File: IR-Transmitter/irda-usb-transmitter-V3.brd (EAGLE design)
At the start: 65.6 x 51 mm, 24 parts, among them IC1 7805, Q2 7.3728MHz, U1 FT232RL, U2 MCP2120

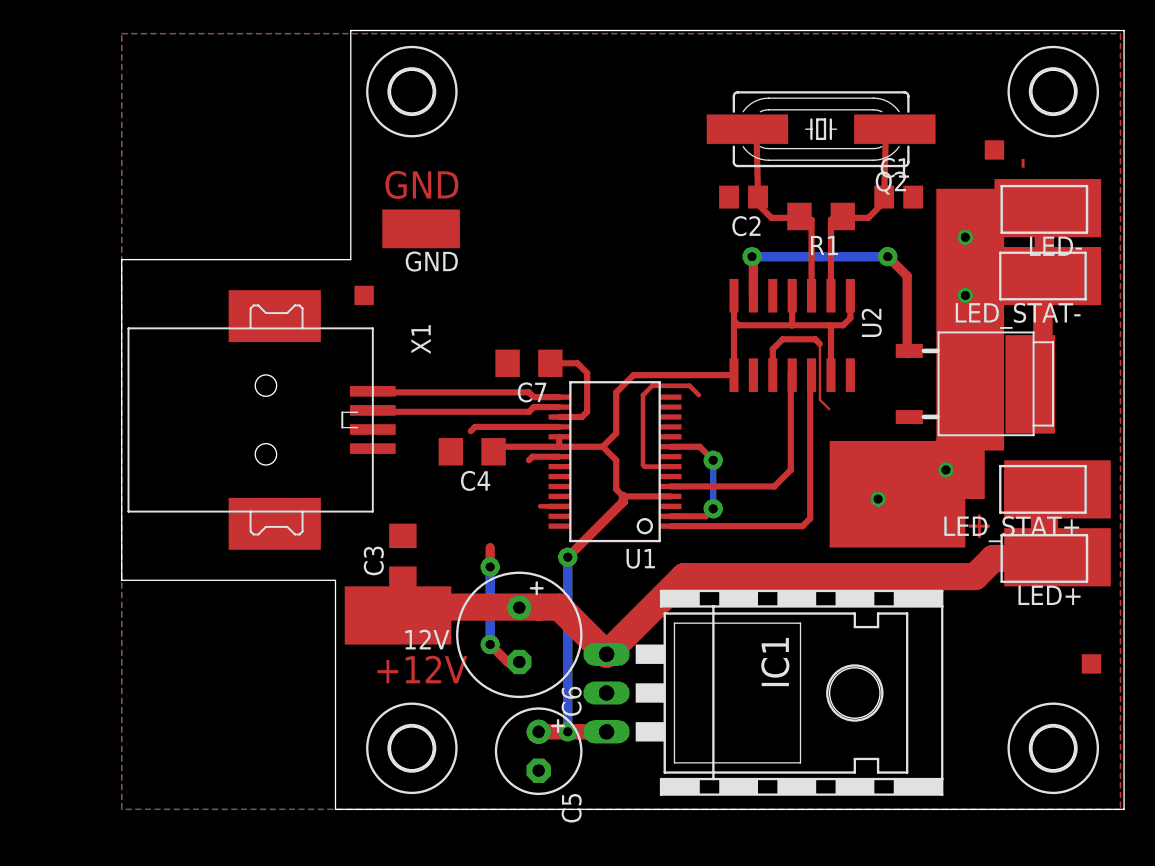
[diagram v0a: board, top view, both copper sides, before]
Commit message: Changed size of IR_Transmitter to fit dirtypcbs.com 50x50mm size.
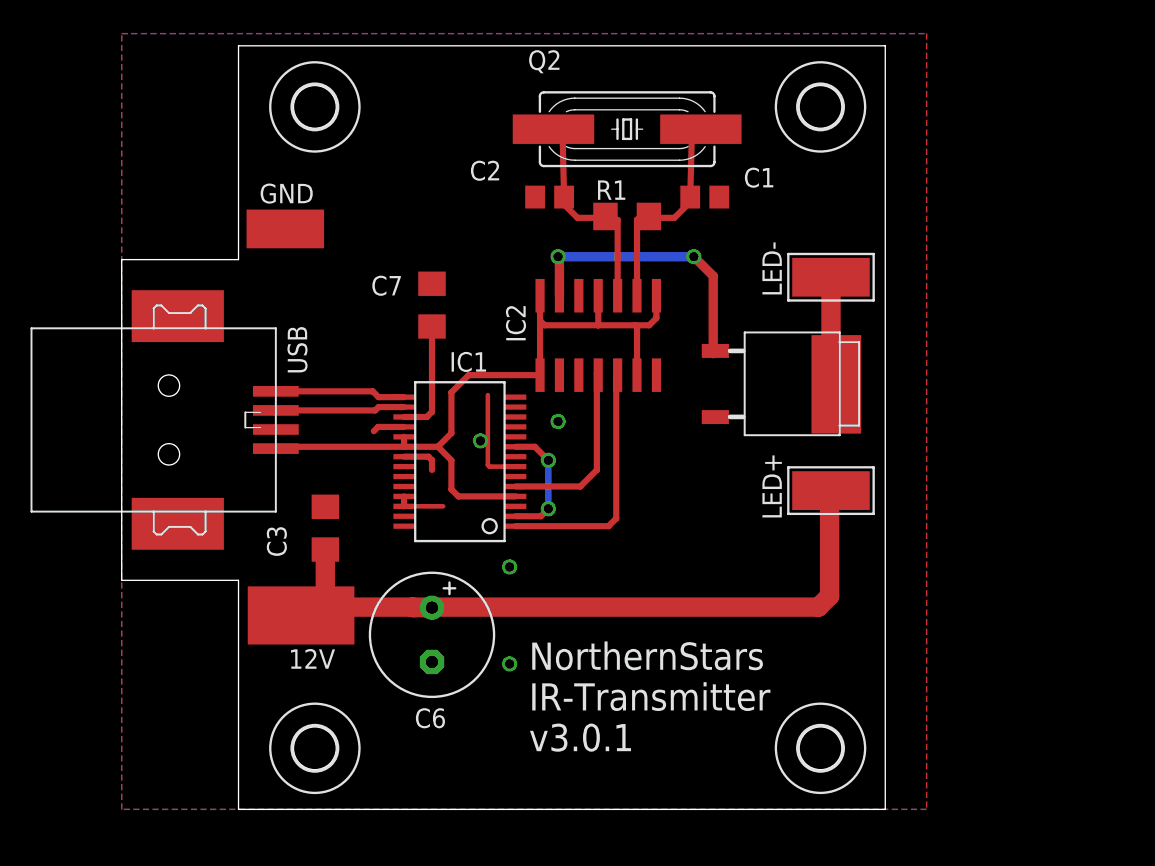
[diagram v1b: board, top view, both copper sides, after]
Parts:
- removed C4: 100n, rcl:C1206
- removed C5: 4µ7, rcl:E2,5-6
- removed LED_STAT+, LED_STAT-: IR-LED, wirepad:5-2,5
- removed U1: FT232RL, ftdichip-3:SSOP28DB
- removed U2: MCP2120, microchip:SO-14
- removed X1: (no value), con-usb-3:USB-B-SMT
- added IC2: MCP2120, microchip:SO-14
- added USB: (no value), con-usb-3:USB-B-SMT
- IC1: value 7805 -> FT232RL; device 78xx_with_heatsink:78XXH -> ftdichip-3:SSOP28DB
- moved IC1 21.1 mm to (22.1, 22.8), turned to 90 degrees
- moved H1 15.3 mm to (45.8, 46.0)
- moved H4 15.2 mm to (45.8, 4.00)
- moved LED+ 14.7 mm to (46.4, 20.9)
- moved LED- 14.7 mm to (46.4, 34.8)
- moved C1 12.7 mm to (38.2, 40.1)
- moved C2 12.7 mm to (28.0, 40.1)
- moved Q2 12.7 mm to (33.1, 44.5)
- moved R1 12.7 mm to (33.1, 38.8)
- moved U$1 12.7 mm to (43.9, 27.9)
- moved GND 8.89 mm to (10.7, 38.0)
- moved C7 7.41 mm to (20.3, 33.0), turned to 90 degrees
- moved H2 6.43 mm to (12.7, 46.0)
- moved 12V 6.35 mm to (12.6, 13.2)
- moved H3 6.35 mm to (12.7, 4.00)
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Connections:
- net +12V: no longer IC1.IN, LED_STAT+.1
- net +3V3: now also IC1.17; no longer U1.17
- net D+: now also IC1.15, USB.D+; no longer U1.15, X1.D+
- net D-: now also IC1.16, USB.D-; no longer U1.16, X1.D-
- net GND: now also IC1.18, IC1.21, IC1.25, IC1.26, IC1.7, IC2.10, IC2.14, IC2.5, IC2.9, USB.GND; no longer C4.2, C5.-, IC1.GND, U1.18, U1.21, U1.25, U1.26, U1.7, U2.10, U2.14, U2.5, U2.9, X1.GND
- net IRLEDS-: no longer LED_STAT-.1
- net N$13: now also IC2.3; no longer U2.3
- net N$3: now also IC1.2, IC1.9; no longer U1.2, U1.9
- net N$9: now also IC2.2; no longer U2.2
- net RX: now also IC1.5, IC2.11; no longer U1.5, U2.11
- net TX: now also IC1.1, IC2.12; no longer U1.1, U2.12
- net TXIR: now also IC2.6; no longer U2.6
- net VCC: now also IC1.19, IC1.20, IC1.4, IC2.1, IC2.13, IC2.4, IC2.7, IC2.8, USB.VUSB; no longer C4.1, C5.+, IC1.OUT, U1.19, U1.20, U1.4, U2.1, U2.13, U2.4, U2.7, U2.8
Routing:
- net GND: track 38.3 -> 14.3 mm, vias 2 -> 4
- net VCC: track 68.2 -> 49.0 mm, vias 2 -> 0
- net IRLEDS-: track 16.9 -> 7.16 mm, vias 4 -> 0
- net +12V: track 53.3 -> 47.2 mm
- net D-: track 12.4 -> 8.49 mm
- net D+: track 12.4 -> 8.55 mm
- net TX: track 18.8 -> 16.2 mm
- net RX: track 14.8 -> 12.3 mm
- net N$3: track 9.29 -> 8.02 mm
- added copper zone on layer 16, net GND
- removed copper zone on layer 16, net IRLEDS-
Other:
- board size 65.6 x 51 mm -> 50 x 50 mm
- board text added: "NorthernStars IR-Transmitter v3.0.1"
- board text removed: "+"
- board text removed: "+12V"
- board text removed: "-"
- board text removed: "GND"

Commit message: Added a jumper to switch between USB power and extranl power for IR-Transmitter. Updated README.md
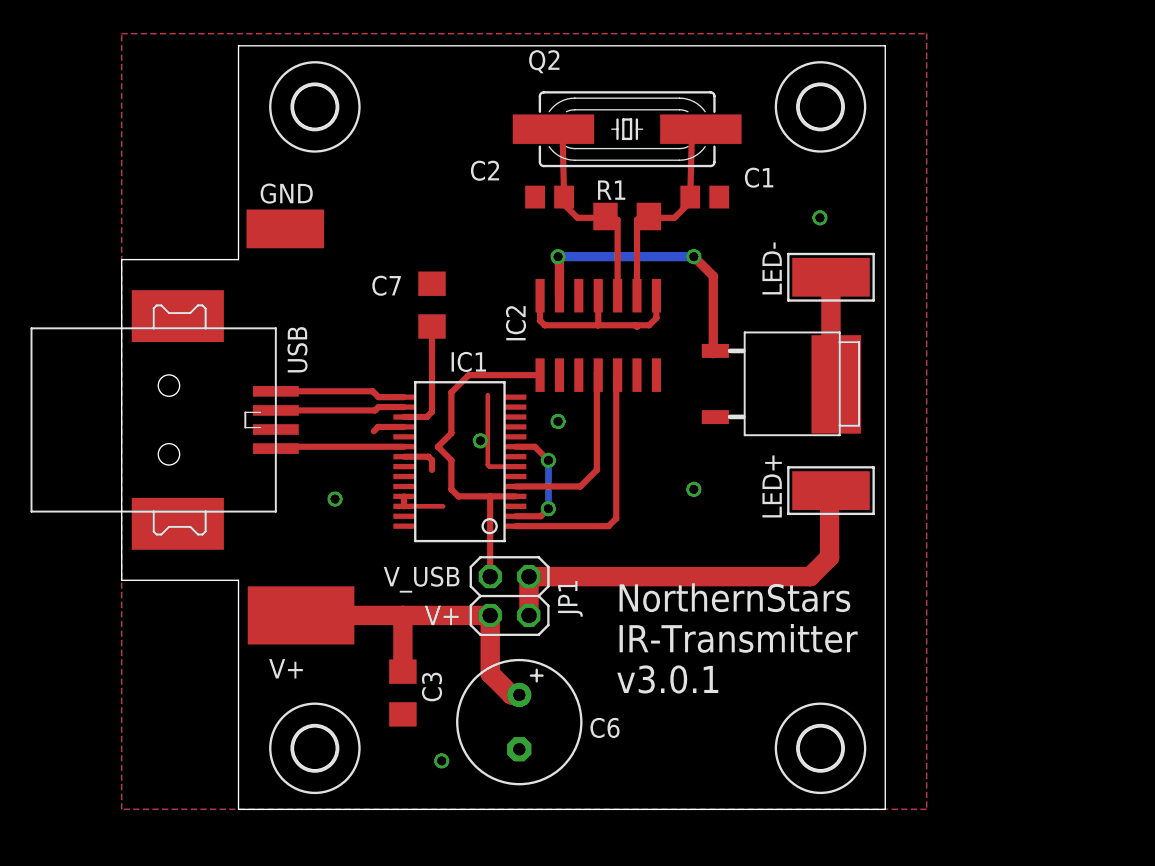
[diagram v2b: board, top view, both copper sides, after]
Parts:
- added JP1: (no value), pinhead:2X02
- moved C3 11.9 mm to (18.4, 7.62), turned to 270 degrees
- moved C6 8.08 mm to (26.0, 5.71)
- renumbered 12V to V+
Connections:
- removed net +12V: C3.1, C6.+, LED+.1, V+.1
- new net V+: C3.1, C6.+, JP1.3, V+.1
- new net VCCIO: IC1.19, IC1.20, IC1.4, IC2.1, IC2.13, IC2.4, IC2.7, IC2.8, JP1.1, USB.VUSB
- net VCC: now also JP1.2, JP1.4, LED+.1; no longer IC1.19, IC1.20, IC1.4, IC2.1, IC2.13, IC2.4, IC2.7, IC2.8, USB.VUSB
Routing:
- net +12V: track 47.2 -> 0.00 mm
- net VCCIO: track 0.00 -> 44.5 mm
- net V+: track 0.00 -> 22.0 mm
- net VCC: track 49.0 -> 27.2 mm
- net GND: vias 4 -> 6
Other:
- board text added: "V+"
- board text added: "V_USB"
